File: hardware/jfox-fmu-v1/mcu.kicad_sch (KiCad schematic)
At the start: 1 part, among them U10 STM32H753IIT6

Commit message: The MCU power rail was drawn, not connected
Fourteen of the STM32H753's VDD pins were floating. The netlist put exactly
three U10 pins on +3V3: 6, 114 and 171 - the two pins at the ends of the rail
wire, plus PDR_ON on its own label. Everything between them was unconnected.

The cause is the fix from three commits ago. Joining same-net pins into a rail
was right; drawing a wire across their stub ends and stopping there was not.
KiCad does not connect a wire to another wire because one's endpoint lies on
it - crossings are crossings, and a T needs an explicit junction. The rail
therefore joined its own two endpoints and ran past the other fourteen taps.

It plots as an unmistakably connected power rail. It looked right in the PDF,
it looked right in the editor, and only the netlist disagreed. That is the
whole lesson: drawings can lie, netlists are what the board is made from.

The ground rail escaped by accident - the STM32 symbol stacks its VSS pins at
one location, so a single stub caught all thirteen. Had the VDD pins been
stacked too, this would have shipped.

gen_fmu_schematic now emits a junction at every intermediate tap.
check_fmu_schematic gains an eighth check that reads the PROJECT netlist and
asserts all 26 MCU supply pins land on their rail - and it had its own version
of the same mistake on the first run, reading the sensor sheet's netlist,
which does not contain U10 at all and so reported every pin missing on a
correct board. Negative-tested by stripping the 25 junctions back out: it
names all fourteen VDD pins and all twelve VSS pins.

Also added the reset circuit, which did not exist. NRST and BOOT0 were both
inputs with nothing driving them. NRST has an internal 30-50k pull-up
(DM00388325 s6.3.16 table 54) so it needs only the external capacitor from
figure 22; BOOT0 has no internal pull and gets 10k to ground, or a marginal
power-up can boot the system bootloader instead of flash.

Checked and NOT changed: VCAP1 and VCAP2 are tied. ERC flags it as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
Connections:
- net +3V3: now also U10.103 (VDD), U10.127 (VDD), U10.136 (VDD), U10.149 (VDD), U10.15 (VDD), U10.159 (VDD), U10.172 (VDD), U10.23 (VDD), U10.36 (VDD), U10.49 (VDD), U10.62 (VDD), U10.72 (VDD), U10.82 (VDD), U10.91 (VDD)
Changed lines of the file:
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@@
 		(instances
 			(project "jfox-fmu"
-				(path "/9d881c85-a00c-43a8-a567-fbff805543dd"
+				(path "/3f27fc2b-d54b-4ad3-8efd-35411c330cc3"
 					(reference "U10")
 					(unit 1)
@@
 		)
 	)
+	(junction
+		(at 85.09 13.97)
+		(diameter 0)
+		(color 0 0 0 0)
+	)
+	(junction
+		(at 87.63 13.97)
+		(diameter 0)
+		(color 0 0 0 0)
+	)
+	(junction
+		(at 90.17 13.97)
+		(diameter 0)
+		(color 0 0 0 0)
+	)
+	(junction
+		(at 92.71 13.97)
+		(diameter 0)
+		(color 0 0 0 0)
+	)
+	(junction
+		(at 95.25 13.97)
+		(diameter 0)
+		(color 0 0 0 0)
+	)
+	(junction
+		(at 97.79 13.97)
+		(diameter 0)
+		(color 0 0 0 0)
+	)
+	(junction
+		(at 100.33 13.97)
+		(diameter 0)
+		(color 0 0 0 0)
+	)
+	(junction
+		(at 102.87 13.97)
+		(diameter 0)
+		(color 0 0 0 0)
+	)
+	(junction
+		(at 105.41 13.97)
+		(diameter 0)
+		(color 0 0 0 0)
+	)
+	(junction
+		(at 107.95 13.97)
+		(diameter 0)
+		(color 0 0 0 0)
+	)
+	(junction
+		(at 110.49 13.97)
+		(diameter 0)
+		(color 0 0 0 0)
+	)
+	(junction
+		(at 113.03 13.97)
+		(diameter 0)
+		(color 0 0 0 0)
+	)
+	(junction
+		(at 115.57 13.97)
+		(diameter 0)
+		(color 0 0 0 0)
+	)
+	(junction
+		(at 118.11 13.97)
+		(diameter 0)
+		(color 0 0 0 0)
+	)
 	(global_label "+3V3"
 		(shape input)
@@
 		)
 	)
+	(junction
+		(at 102.87 247.65)
+		(diameter 0)
+		(color 0 0 0 0)
+	)
+	(junction
+		(at 102.87 247.65)
+		(diameter 0)
+		(color 0 0 0 0)
+	)
+	(junction
+		(at 102.87 247.65)
+		(diameter 0)
+		(color 0 0 0 0)
+	)
+	(junction
+		(at 102.87 247.65)
+		(diameter 0)
+		(color 0 0 0 0)
+	)
+	(junction
+		(at 102.87 247.65)
+		(diameter 0)
+		(color 0 0 0 0)
+	)
+	(junction
+		(at 102.87 247.65)
+		(diameter 0)
+		(color 0 0 0 0)
+	)
+	(junction
+		(at 102.87 247.65)
+		(diameter 0)
+		(color 0 0 0 0)
+	)
+	(junction
+		(at 102.87 247.65)
+		(diameter 0)
+		(color 0 0 0 0)
+	)
+	(junction
+		(at 102.87 247.65)
+		(diameter 0)
+		(color 0 0 0 0)
+	)
+	(junction
+		(at 102.87 247.65)
+		(diameter 0)
+		(color 0 0 0 0)
+	)
+	(junction
+		(at 102.87 247.65)
+		(diameter 0)
+		(color 0 0 0 0)
+	)
 	(global_label "GND"

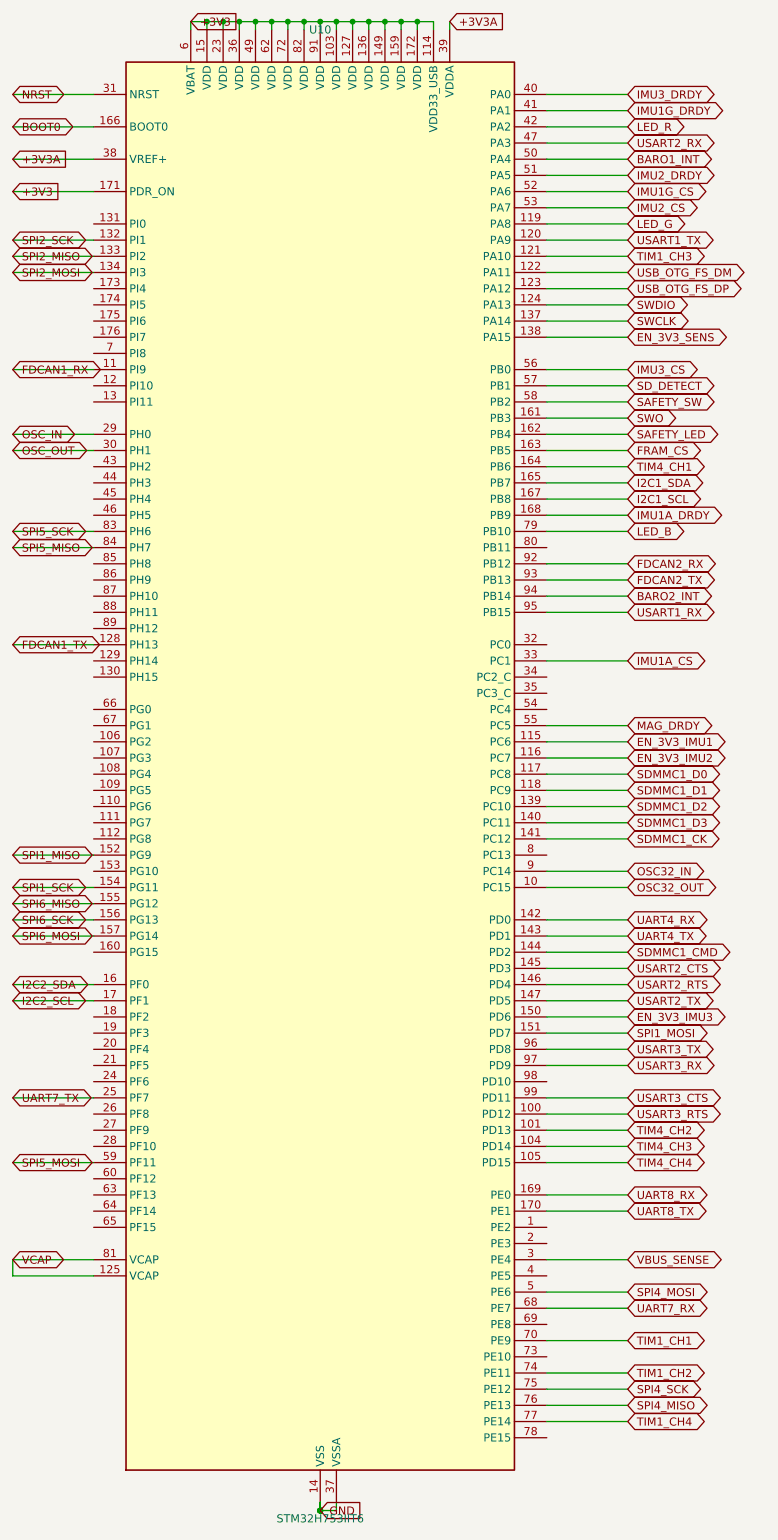
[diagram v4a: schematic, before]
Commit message: Five connections that went nowhere, and the pin name that hid one
None of these were visible as failures. Every one was a wire drawn to a name
that did not exist, which KiCad accepts silently.

wire_part matches by pin NAME. Four keys in the comms sheet matched nothing:

  "DAT3/CS"  the microSD symbol's pin is "CD/DAT3", so SDMMC1_D3 reached the
             MCU and stopped. The card would have run in 1-bit mode at best.
  "DET"      this symbol has no card-detect pin at all, so SD_DETECT had no
             source. Recorded rather than faked - it needs a socket symbol
             that exposes CD.
  "VSS2"     does not exist on this symbol.
  "SBU1/2"   do not exist on the USB-C symbol.

PC2 is the one worth remembering. On this package PC2 and PC3 exist only as
PC2_C and PC3_C - the analog-switch-capable balls. plan_pinout works from the
chip's alternate-function table, which calls them PC2 and PC3, so the lookup
missed and the allocated signal went nowhere. Aliased in both the generator
and the checker, which is what surfaced it: the check reported "symbol has no
pin named PC2" the moment the allocation grew enough to reach that pin.

Four parts that were missing outright, each leaving a function non-functional:

  R9/R10   5.1k on USB CC1/CC2. Without them the port is not a USB-C sink and
           no host will enumerate it. The CC pins reached the connector and
           nothing else.
  R11/R12  VBUS sense divider. VBUS_SENSE reached an ADC pin with nothing
           driving it. 10k/10k puts 5.25 V at 2.63 V, inside the reference.
  R13-R16  pull-ups on the four load-switch fault outputs, which are open
           drain and were unreadable without them.

And ten status signals now reach the MCU that previously reached nothing:
BRICK_VALID, SERVO_VALID, USB_VALID, PG_3V3, the four rail fault flags and
both isolator fault outputs. The board could not previously tell whether its
power source was valid, whether a sensor rail had tripped, or whether an
isolated 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
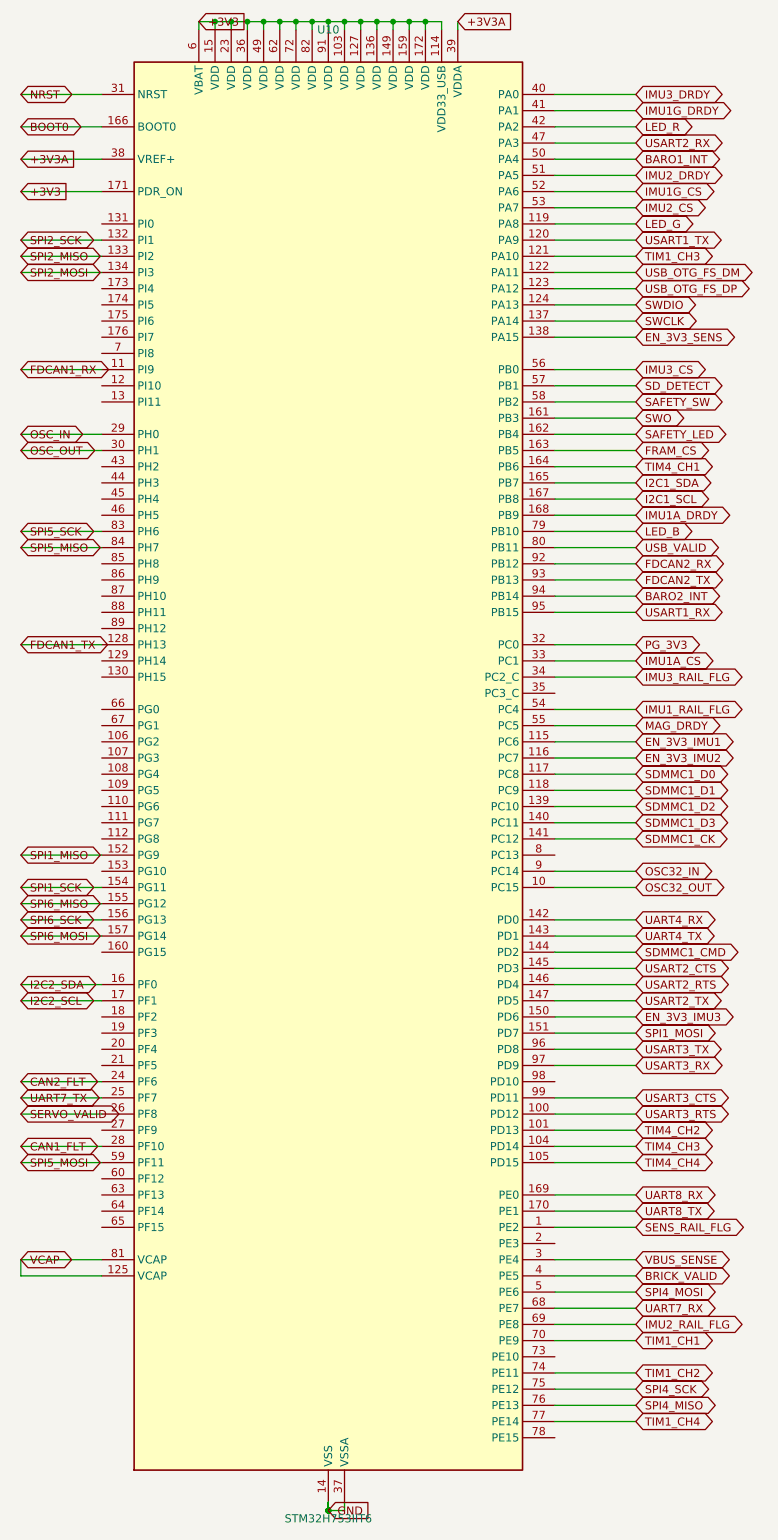
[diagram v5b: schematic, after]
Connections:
- net SENS_RAIL_FLG: now reaches U10.1 (PE2)
- net CAN2_FLT: now reaches U10.24 (PF6)
- net SERVO_VALID: now reaches U10.26 (PF8)
- net CAN1_FLT: now reaches U10.28 (PF10)
- net PG_3V3: now reaches U10.32 (PC0)
- net IMU3_RAIL_FLG: now reaches U10.34 (PC2_C)
- net BRICK_VALID: now reaches U10.4 (PE5)
- net IMU1_RAIL_FLG: now reaches U10.54 (PC4)
- net IMU2_RAIL_FLG: now reaches U10.69 (PE8)
- net USB_VALID: now reaches U10.80 (PB11)
